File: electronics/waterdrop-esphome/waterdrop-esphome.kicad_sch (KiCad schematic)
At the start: 18 parts, among them J1 12V_IN, J2 12V_OUT, J3 Comm_RO, J4 Comm_Faucet, K1 G5LE-1, Q1 BC817, U2 ESP32-S3-Tiny, U3 74AHCT125

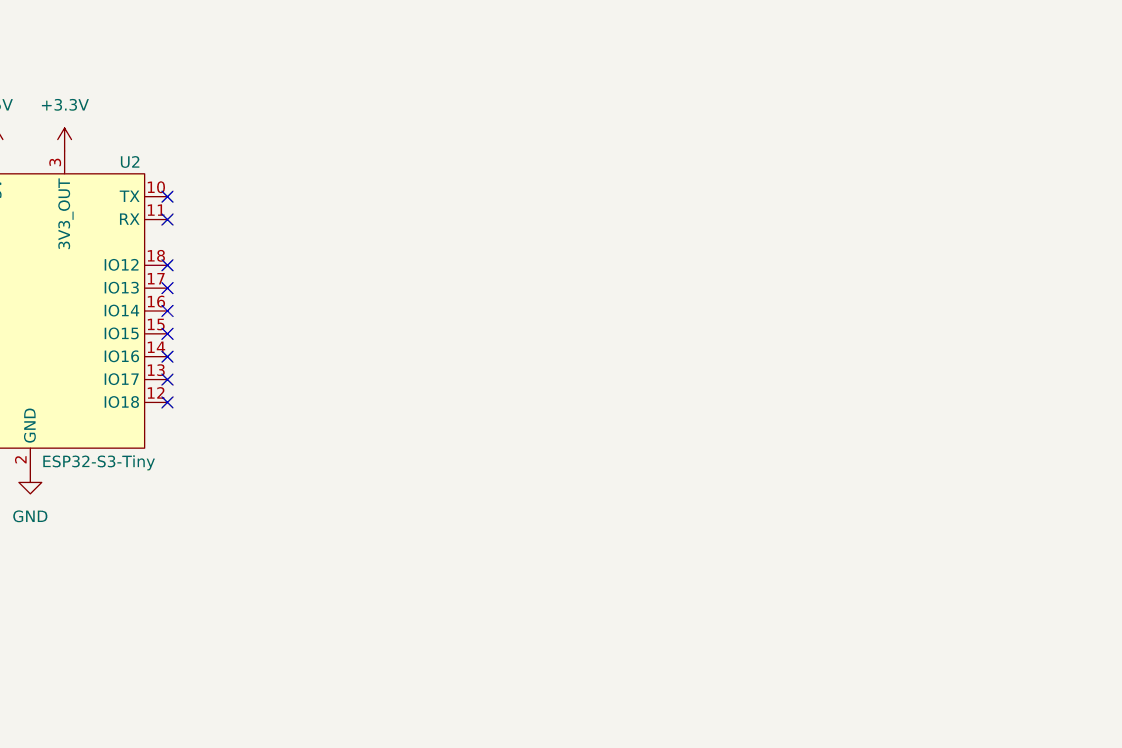
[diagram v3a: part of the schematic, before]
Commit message: Schematics for water valve
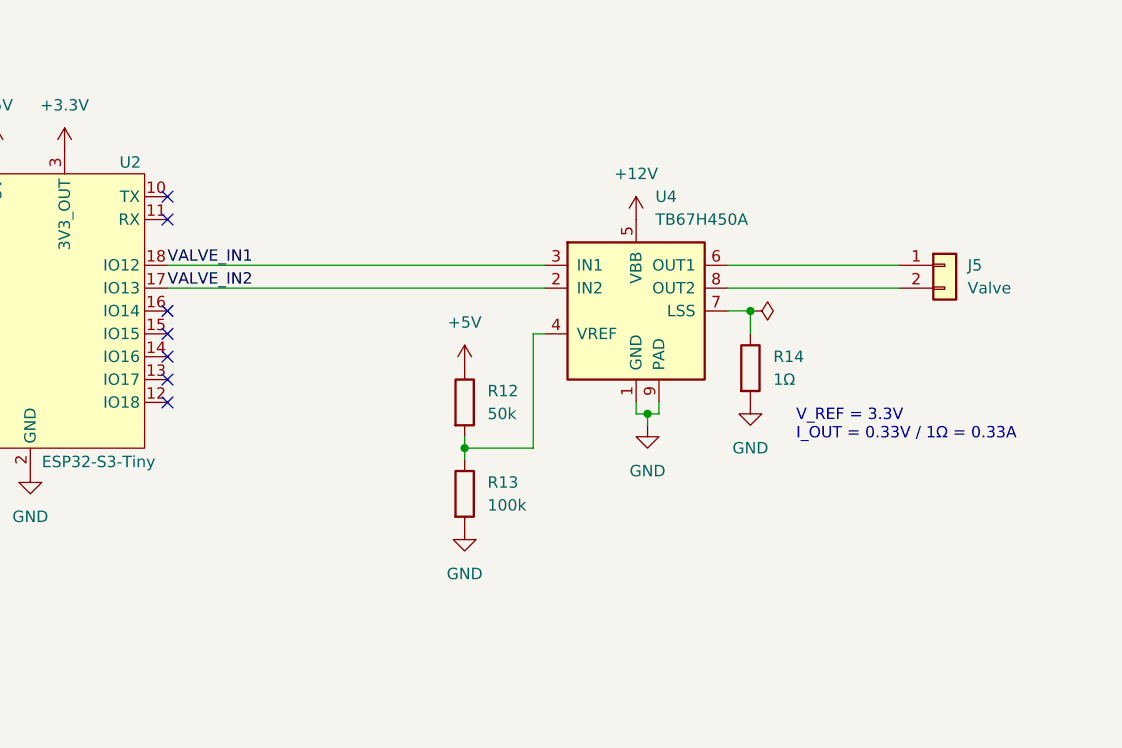
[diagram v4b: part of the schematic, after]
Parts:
- added J5: Valve, symbol Connector_Generic:Conn_01x02
- added R12: 50k, symbol Device:R
- added R13: 100k, symbol Device:R
- added R14: 1Ω, symbol Device:R
- added U4: TB67H450A, Package_SO:SOIC-8-1EP_3.9x4.9mm_P1.27mm_EP2.41x3.3mm, symbol Driver_Motor:A4950E
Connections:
- net +12V: now also U4.5 (VBB)
- net +5V: now also R12.1
- net GND: now also R13.2, R14.2, U4.1 (GND), U4.9 (PAD)
- net VALVE_IN2: now reaches U2.17 (IO13)
- net VALVE_IN2: now also U4.2 (IN2)
- net VALVE_IN1: now reaches U2.18 (IO12)
- net VALVE_IN1: now also U4.3 (IN1)
- new net: J5.1 (Pin_1), U4.6 (OUT1)
- new net: J5.2 (Pin_2), U4.8 (OUT2)
- new net: R12.2, R13.1, U4.4 (VREF)
- new net: R14.1, U4.7 (LSS)
- no-connect marks 19 -> 17
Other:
- note added: "V_REF = 3.3V I_OUT = 0.33V / 1Ω = 0.33A"

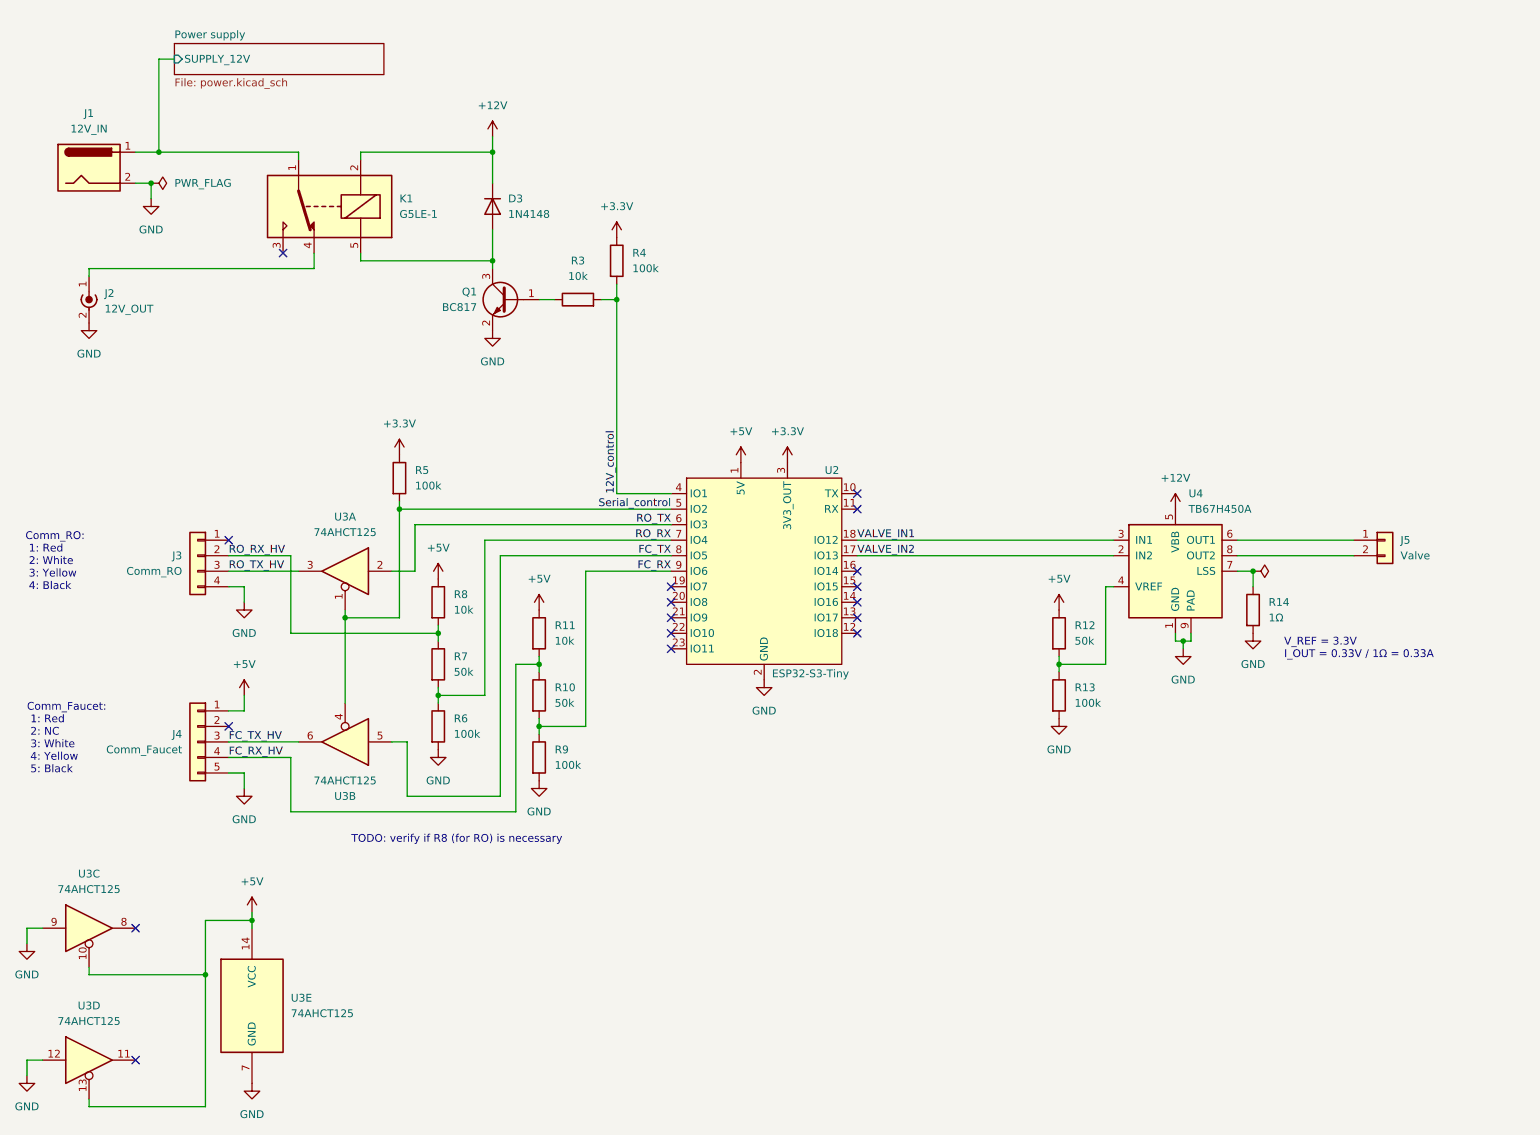
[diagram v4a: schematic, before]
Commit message: Schematics are ready for PCB layout
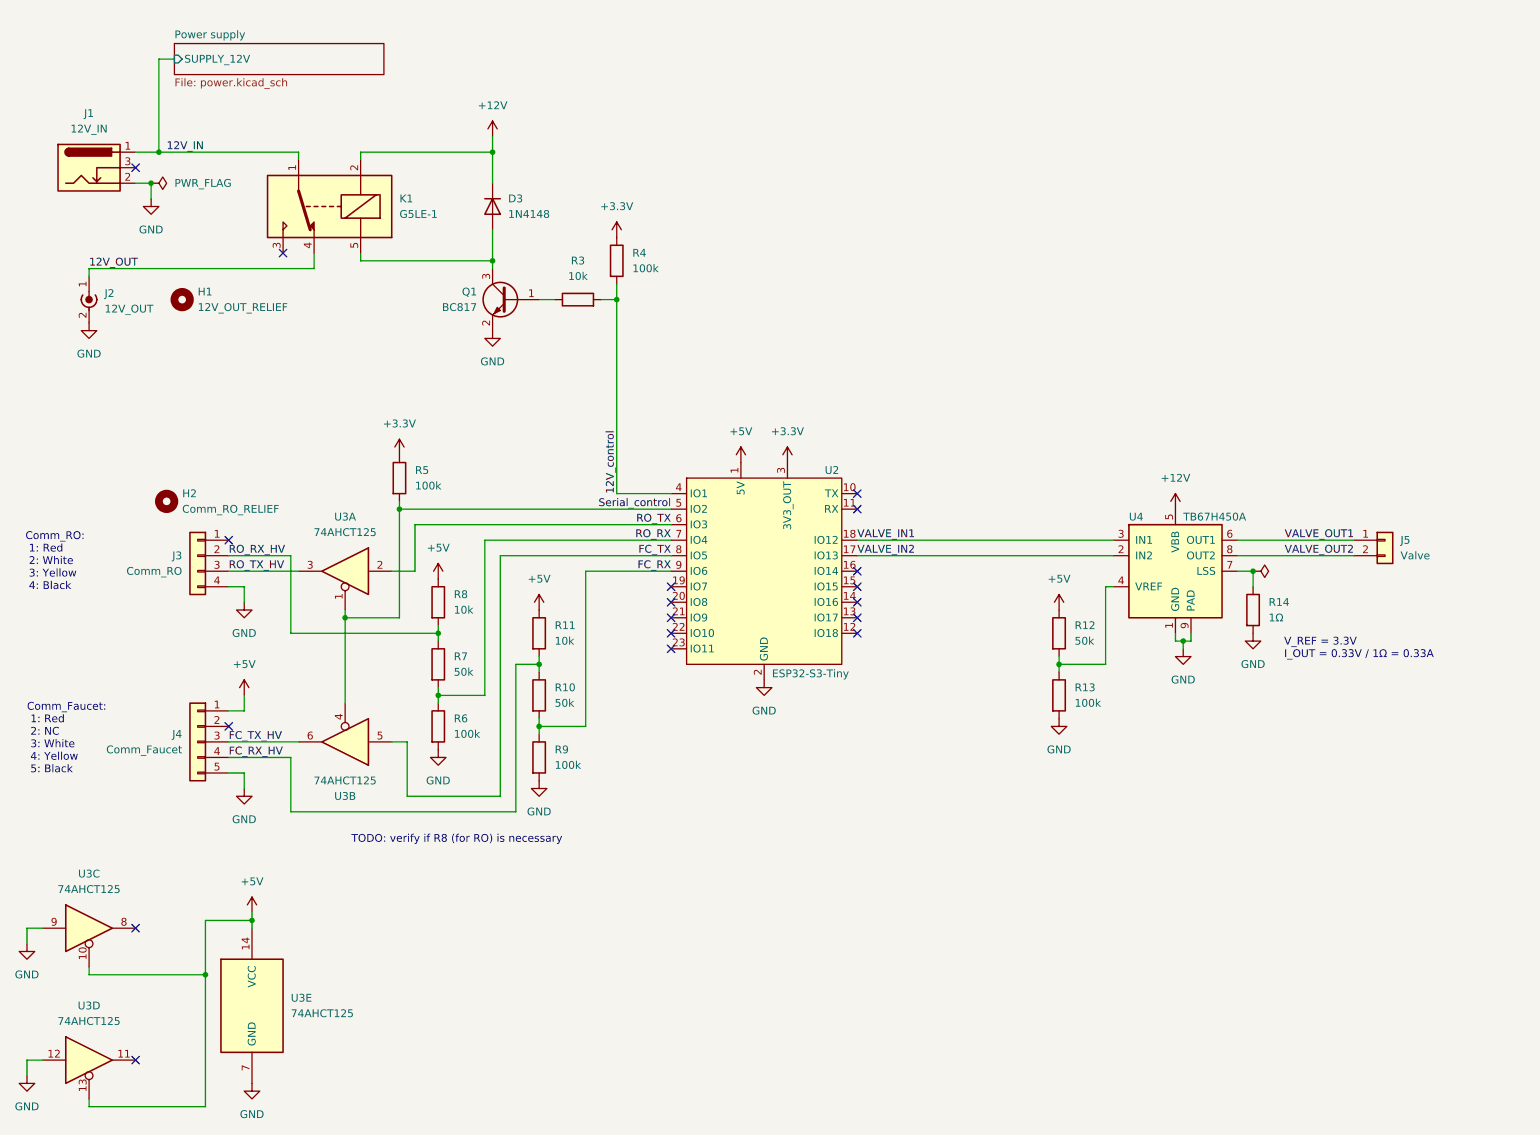
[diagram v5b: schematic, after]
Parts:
- removed J1: 12V_IN, Connector_BarrelJack:BarrelJack_Horizontal, symbol Connector:Barrel_Jack
- added H1: 12V_OUT_RELIEF, MountingHole:MountingHole_4.3mm_M4, symbol Mechanical:MountingHole
- added H2: Comm_RO_RELIEF, MountingHole:MountingHole_4.3mm_M4, symbol Mechanical:MountingHole
- added J1: 12V_IN, Connector_BarrelJack:BarrelJack_Horizontal, symbol Connector:Barrel_Jack_Switch
- D3: footprint Diode_THT:D_DO-35_SOD27_P7.62mm_Horizontal -> Diode_SMD:D_SOD-123
- J2: footprint Connector_Wire:SolderWire-1sqmm_1x02_P5.4mm_D1.4mm_OD2.7mm_Relief -> Connector_Wire:SolderWire-1.5sqmm_1x02_P6mm_D1.7mm_OD3mm_Relief
- J3: footprint (none) -> Connector_Wire:SolderWire-0.25sqmm_1x04_P4.2mm_D0.65mm_OD1.7mm_Relief
- J4: footprint (none) -> Connector_PinHeader_2.54mm:PinHeader_1x05_P2.54mm_Horizontal
- J5: footprint (none) -> Connector_PinHeader_2.54mm:PinHeader_1x02_P2.54mm_Horizontal
- R10, R11, R12, R13, R14, R3, R4, R5, R6, R7, R8, R9: footprint (none) -> Resistor_SMD:R_0805_2012Metric_Pad1.20x1.40mm_HandSolder
- U3: footprint (none) -> Package_SO:SOIC-14_3.9x8.7mm_P1.27mm
- U4: footprint Package_SO:SOIC-8-1EP_3.9x4.9mm_P1.27mm_EP2.41x3.3mm -> Package_SO:SOIC-8-1EP_3.9x4.9mm_P1.27mm_EP2.29x3mm_ThermalVias
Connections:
- net GND: now also J1.2
- net VALVE_OUT1: now reaches J5.1 (Pin_1), U4.6 (OUT1)
- net VALVE_OUT2: now reaches J5.2 (Pin_2), U4.8 (OUT2)
- net 12V_OUT: now reaches J2.1 (In), K1.4
- net Power supply/SUPPLY_12V renamed 12V_IN
- net 12V_IN: now also J1.1
- no-connect marks 17 -> 18

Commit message: PCB: lay out components
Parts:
- added H3, H4: MountingHole, MountingHole:MountingHole_4.3mm_M4, symbol Mechanical:MountingHole
- H1, H2: footprint MountingHole:MountingHole_4.3mm_M4 -> MountingHole_extra:MountingHole_4.3mm
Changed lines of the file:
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@@
 			)
 		)
-		(property "Footprint" "MountingHole:MountingHole_4.3mm_M4"
+		(property "Footprint" "MountingHole_extra:MountingHole_4.3mm"
 			(at 41.91 96.52 0)
 			(effects
@@
 	)
 	(symbol
+		(lib_id "Mechanical:MountingHole")
+		(at 246.38 25.4 0)
+		(unit 1)
+		(exclude_from_sim no)
+		(in_bom no)
+		(on_board yes)
+		(dnp no)
+		(fields_autoplaced yes)
+		(property "Reference" "H4"
+			(at 248.92 24.1299 0)
+			(effects
+				(font
+					(size 1.27 1.27)
+				)
+				(justify left)
+			)
+		)
+		(property "Value" "MountingHole"
+			(at 248.92 26.6699 0)
+			(effects
+				(font
+					(size 1.27 1.27)
+				)
+				(justify left)
+			)
+		)
+		(property "Footprint" "MountingHole:MountingHole_4.3mm_M4"
+			(at 246.38 25.4 0)
+			(effects
+				(font
+					(size 1.27 1.27)
+				)
+				(hide yes)
+			)
+		)
+		(property "Datasheet" "~"
+			(at 246.38 25.4 0)
+			(effects
+				(font
+					(size 1.27 1.27)
+				)
+				(hide yes)
+			)
+		)
+		(property "Description" "Mounting Hole without connection"
+			(at 246.38 25.4 0)
+			(effects
+				(font
+					(size 1.27 1.27)
+				)
+				(hide yes)
+			)
+		)
+		(instances
+			(project ""
+				(path "/35f74f22-9f08-4dab-aa3a-794dd2e7ee12"
+					(reference "H4")
+					(unit 1)
+				)
+			)
+		)
+	)
+	(symbol
 		(lib_id "Device:R")
 		(at 109.22 63.5 90)
@@
 	)
 	(symbol
+		(lib_id "Mechanical:MountingHole")
+		(at 246.38 19.05 0)
+		(unit 1)
+		(exclude_from_sim no)
+		(in_bom no)
+		(on_board yes)
+		(dnp no)
+		(fields_autoplaced yes)
+		(property "Reference" "H3"
+			(at 248.92 17.7799 0)
+			(effects
+				(font
+					(size 1.27 1.27)
+				)
+				(justify left)
+			)
+		)
+		(property "Value" "MountingHole"
+			(at 248.92 20.3199 0)
+			(effects
+				(font
+					(size 1.27 1.27)
+				)
+				(justify left)
+			)
+		)
+		(property "Footprint" "MountingHole:MountingHole_4.3mm_M4"
+			(at 246.38 19.05 0)
+			(effects
+				(font
+					(size 1.27 1.27)
+				)
+				(hide yes)
+			)
+		)
+		(property "Datasheet" "~"
+			(at 246.38 19.05 0)
+			(effects
+				(font
+					(size 1.27 1.27)
+				)
+				(hide yes)
+			)
+		)
+		(property "Description" "Mounting Hole without connection"
+			(at 246.38 19.05 0)
+			(effects
+				(font
+					(size 1.27 1.27)
+				)
+				(hide yes)
+			)
+		)
+		(instances
+			(project ""
+				(path "/35f74f22-9f08-4dab-aa3a-794dd2e7ee12"
+					(reference "H3")
+					(unit 1)
+				)
+			)
+		)
+	)
+	(symbol
 		(lib_id "power:GND")
 		(at 55.88 191.77 0)
@@
 			)
 		)
-		(property "Footprint" "MountingHole:MountingHole_4.3mm_M4"
+		(property "Footprint" "MountingHole_extra:MountingHole_4.3mm"
 			(at 44.45 63.5 0)
 			(effects
